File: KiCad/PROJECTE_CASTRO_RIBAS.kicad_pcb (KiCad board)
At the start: 2 copper layers, 138.5 x 88.9 mm, 63 parts, among them J1 DE9_Pins, J2 DE9_Pins, J4 Conn_01x02_Pin, K1 Fujitsu_FTR-LYAA005x, K2 Fujitsu_FTR-LYAA005x, SW3 SW_Push_Dual, SW4 SW_Push, SW5 SW_Push, U1 LM2596S-12, U2 LM1117DT-3.3, U20 PIC24HJ128GP502, U23 FXTH87, U3 SN65HVD230, U4 MAX3232, Y1 Crystal

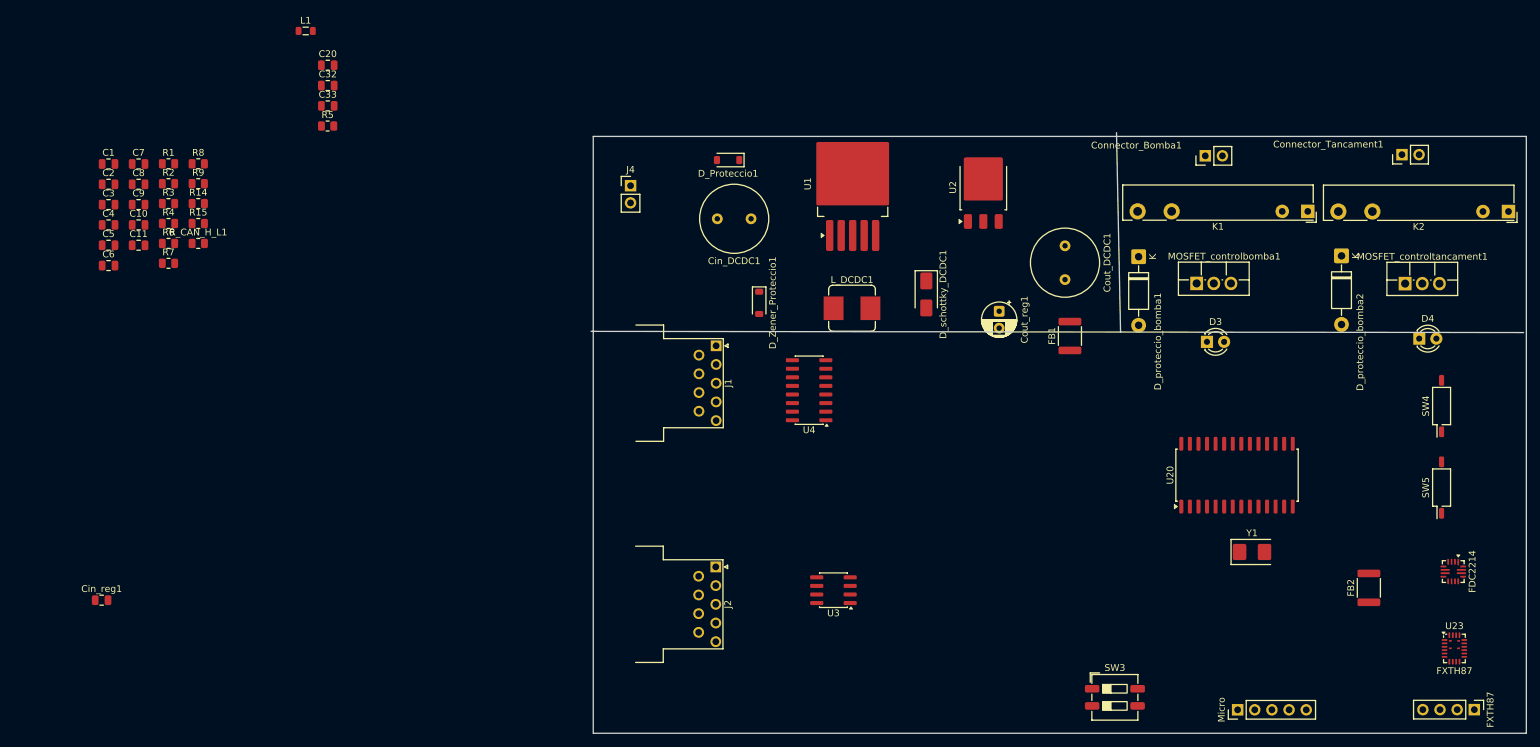
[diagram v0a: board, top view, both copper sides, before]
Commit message: Readme alguns proveïdors i foto del diagrama de blocs
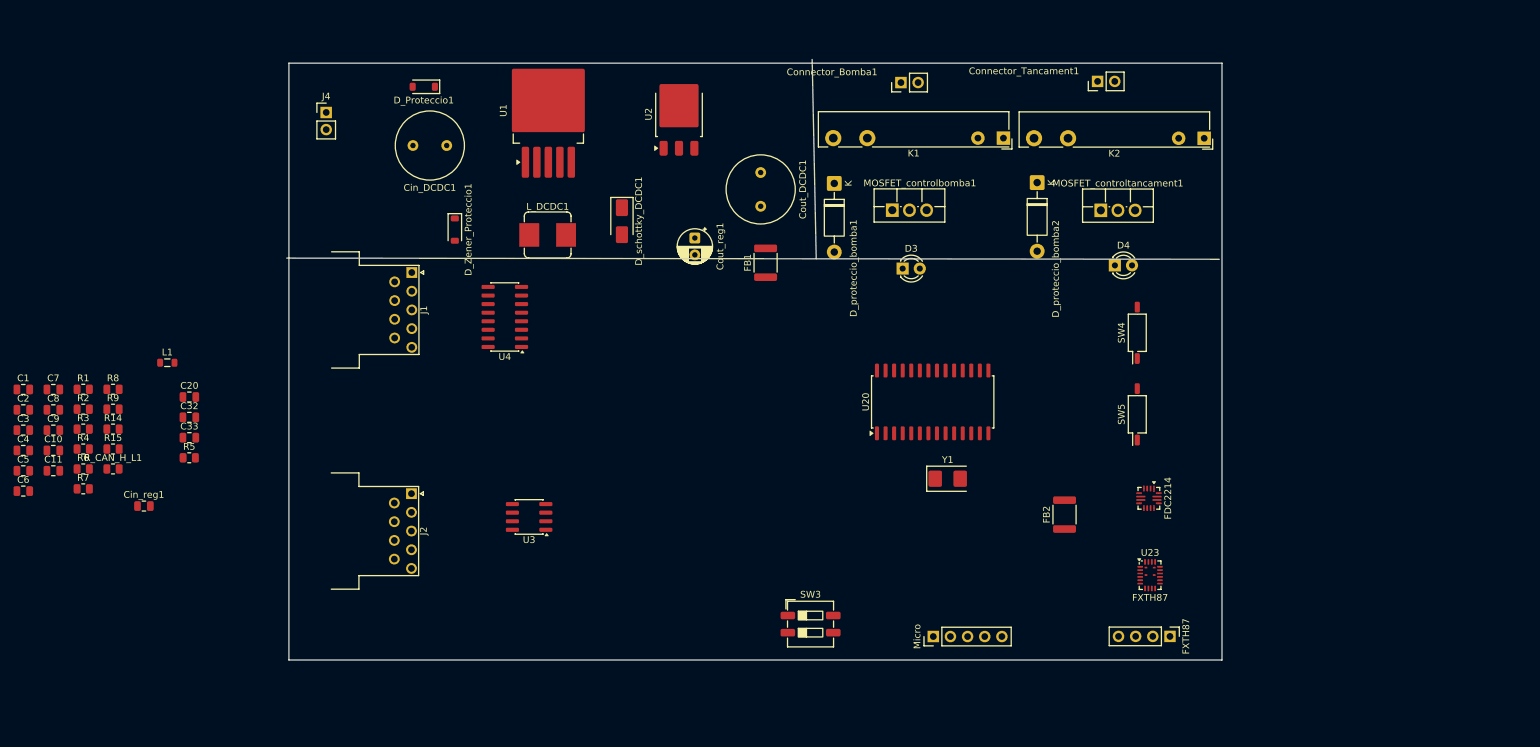
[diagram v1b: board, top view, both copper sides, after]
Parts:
- moved C20 53.2 mm to (77.6, 93.4)
- moved R5 53.2 mm to (77.5, 102.4)
- moved C33 53.2 mm to (77.6, 99.4)
- moved C32 53.2 mm to (77.6, 96.4)
- moved L1 53.2 mm to (74.3, 88.3)
- moved Connector_Bomba1 46.4 mm to (182.9, 46.8)
- moved D3 46.4 mm to (183.2, 74.4)
- moved D_proteccio_bomba1 46.4 mm to (173.1, 61.8)
- moved FXTH87 46.4 mm to (222.8, 128.8)
- moved MOSFET_controlbomba1 46.4 mm to (181.7, 65.7)
- moved U1 46.4 mm to (130.7, 51.0)
- moved U2 46.4 mm to (150.1, 51.5)
- moved U23 46.4 mm to (219.8, 119.8)
- moved Cin_DCDC1 46.4 mm to (115.7, 56.1)
- moved J1 46.4 mm to (110.5, 75.0)
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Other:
- outline, holes or cut-outs redrawn

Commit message: ALFRED DEGANOS SECOOOOS PLS DADDY ALFRED TE CAMELAMOS
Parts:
- removed FXTH87: Conn_01x04_Pin, Connector_PinHeader_2.54mm:PinHeader_1x04_P2.54mm_Vertical
- added J5: Conn_01x04_Pin, Connector_PinHeader_2.54mm:PinHeader_1x04_P2.54mm_Vertical, F.Cu at (61.9, 63.7)
- added TP1: Tp_3.3V, TestPoint:TestPoint_Keystone_5015_Micro_Mini, F.Cu at (55.0, 63.3)
- added TP2: Tp_5V, TestPoint:TestPoint_Keystone_5015_Micro_Mini, F.Cu at (55.0, 67.1)
- added TP3: Tp_12V, TestPoint:TestPoint_Keystone_5015_Micro_Mini, F.Cu at (55.0, 70.8)
- added TP4: Tp_Osc_IN, TestPoint:TestPoint_Keystone_5015_Micro_Mini, F.Cu at (69.7, 77.5)
- added TP5: Tp_Osc_OUT, TestPoint:TestPoint_Keystone_5015_Micro_Mini, F.Cu at (69.7, 81.3)
- added TP6: Tp_GND, TestPoint:TestPoint_Keystone_5015_Micro_Mini, F.Cu at (55.0, 74.6)
- added TP7: Tp_GNDPWR, TestPoint:TestPoint_Keystone_5015_Micro_Mini, F.Cu at (55.0, 78.3)
- added TP8: Tp_12V_Bomba, TestPoint:TestPoint_Keystone_5015_Micro_Mini, F.Cu at (62.3, 77.5)
- added TP9: Tp_12V_Tancament, TestPoint:TestPoint_Keystone_5015_Micro_Mini, F.Cu at (62.3, 81.3)
- moved FB2 147.1 mm to (67.7, 63.9), turned to 0 degrees
- moved Cin_reg1 104.6 mm to (156.4, 49.4)
- moved SW5 63.1 mm to (161.5, 124.2), turned to 180 degrees
- moved SW4 60.2 mm to (173.4, 124.5), turned to 180 degrees
- moved K2 56.4 mm to (198.8, 103.5), turned to 90 degrees
- moved J3 52.3 mm to (135.6, 124.8)
- moved SW3 43.8 mm to (126.0, 123.0)
- moved Connector_Tancament1 41.3 mm to (207.2, 87.7), turned to 0 degrees
- moved D4 38.3 mm to (180.0, 90.2), turned to -90 degrees
- moved U20 37.9 mm to (149.8, 93.8)
- moved Y1 37.9 mm to (152.0, 105.2)
- moved MOSFET_controltancament1 33.1 mm to (188.2, 88.2), turned to -90 degrees
- moved U6 29.9 mm to (191.9, 119.5), turned to 0 degrees
- moved Cin_DCDC1 29.5 mm to (142.8, 68.0)
- moved Connector_Bomba1 26.8 mm to (207.1, 58.6), turned to 0 degrees
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- renumbered Micro to J3, FDC2214 to U6
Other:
- board size 138.5 x 88.9 mm -> 114.1 x 85.8 mm
